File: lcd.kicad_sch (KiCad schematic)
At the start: 1 part, among them J4 Conn_01x12

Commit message: version 4: changed GPIO expander, added current sense resistor to electrodes, added buzzer pins, fixed some gpio inputs that needs to be pulled high, added battery charge detection, added battery level measurement feature
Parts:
- J4: Long Description (none) -> 1.28 inch Round LCD with GCA
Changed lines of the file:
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@@
+      (effects (font (size 1.27 1.27)) hide)
+    )
+    (property "Description" "1.28 inch LCD round screen" (at 124.46 80.01 0)
+      (effects (font (size 1.27 1.27)) hide)
+    )
+    (property "Long Description" "1.28 inch Round LCD with GCA" (at 124.46 80.01 0)
       (effects (font (size 1.27 1.27)) hide)
     )

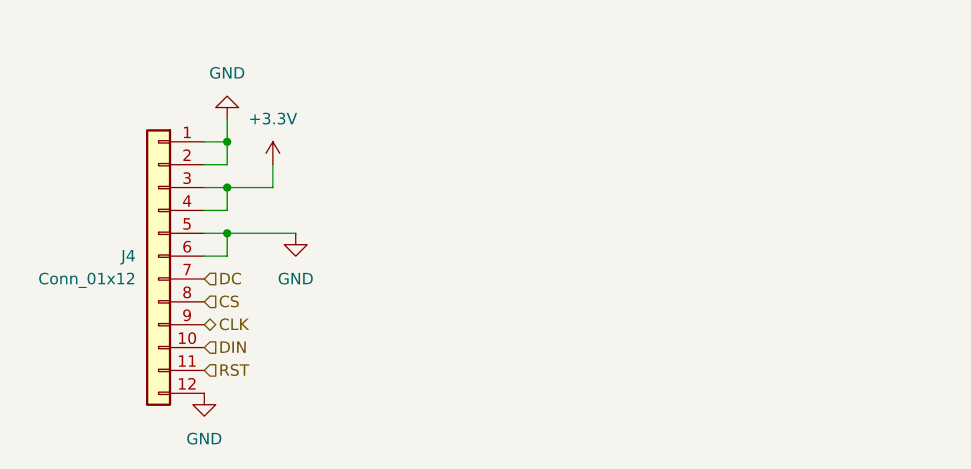
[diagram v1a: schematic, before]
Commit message: version 5: replaced ESP32-WROVER module with ESP-Mini, removed 2.5mm plugs, changed USB connector and routed electrode signals on it, added RC snubber circuit to boost converter and output caps to reduce switching loop
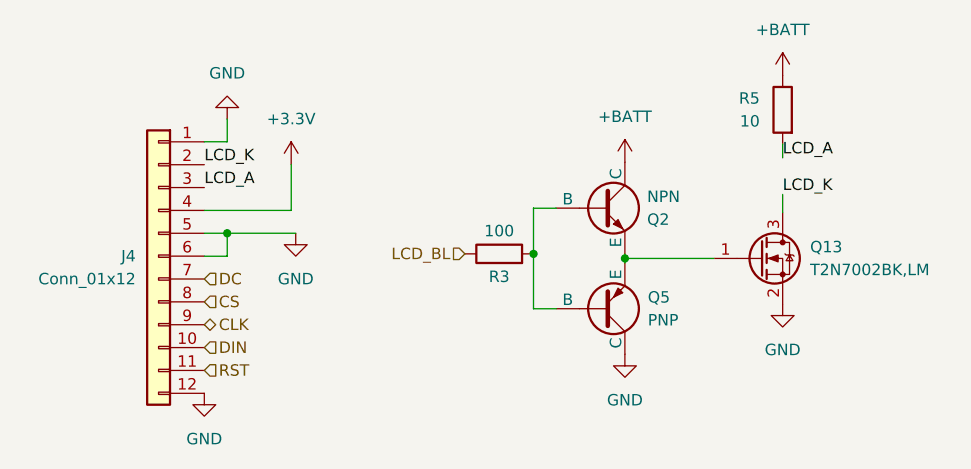
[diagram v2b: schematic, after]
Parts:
- added Q13: T2N7002BK,LM, Package_TO_SOT_SMD:SOT-23, symbol Transistor_FET:TSM2302CX
- added Q2: NPN, Package_TO_SOT_SMD:SOT-23, symbol Simulation_SPICE:NPN
- added Q5: PNP, Package_TO_SOT_SMD:SOT-23, symbol Simulation_SPICE:PNP
- added R3: 100, Resistor_SMD:R_0402_1005Metric, symbol Device:R
- added R5: 10, Resistor_SMD:R_0402_1005Metric, symbol Device:R
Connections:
- net +3.3V: no longer J4.3 (Pin_3)
- net GND: now also Q13.2 (S), Q5.3 (C); no longer J4.2 (Pin_2)
- new net: Q2.1 (B), Q5.1 (B), R3.2
- new net: Q13.1 (G), Q2.2 (E), Q5.2 (E)
- new net +BATT: Q2.3 (C), R5.1
- new net LCD_A: J4.3 (Pin_3), R5.2
- new net LCD_BL: R3.1
- new net LCD_K: J4.2 (Pin_2), Q13.3 (D)
